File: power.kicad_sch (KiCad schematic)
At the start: 27 parts, among them Q1 CSD17311Q5, Q2 CSD17311Q5, U10 DS4432U+, U9 TPS40305

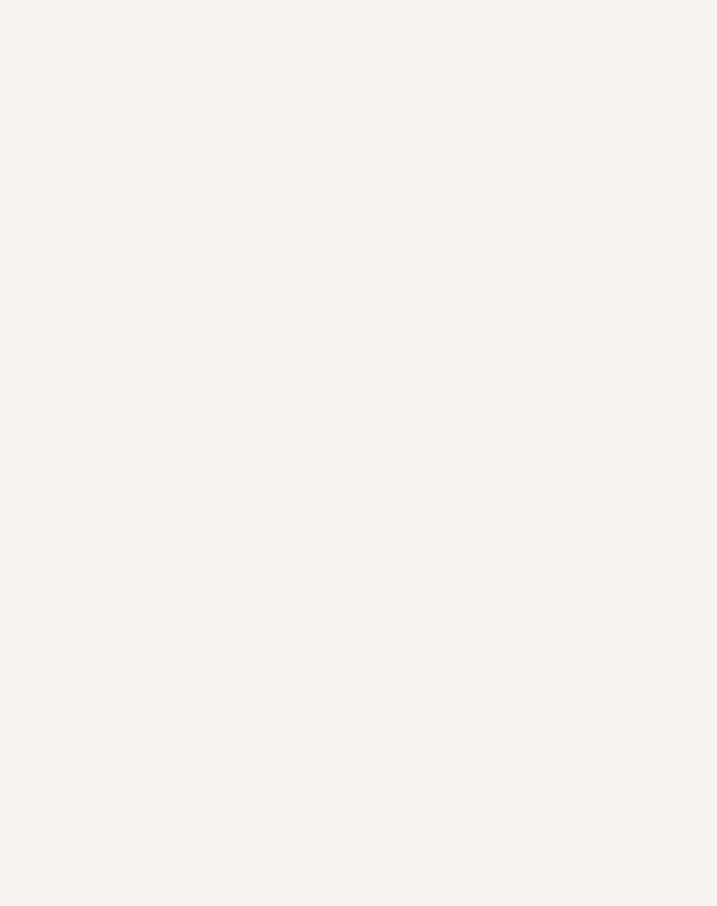
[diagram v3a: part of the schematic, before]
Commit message: started on new LM5085 based buck design
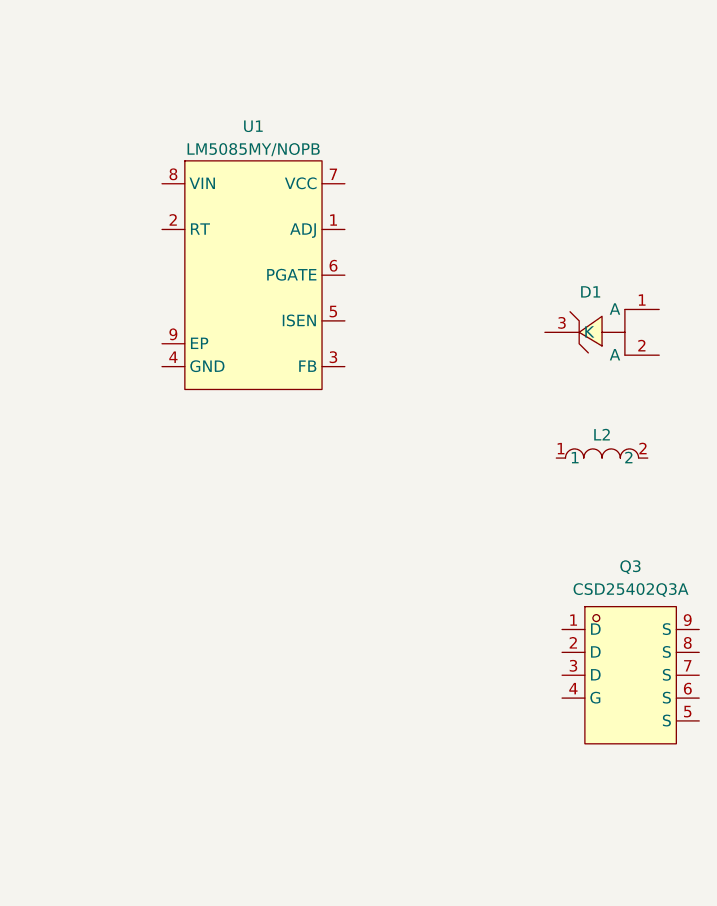
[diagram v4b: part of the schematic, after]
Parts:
- added D1: FSV1045V, lcsc:TO-277A_L6.1-W4.6-P2.13-LS6.5-TR, symbol lcsc:FSV1045V
- added L2: IHLP4040DZER1R0M01, lcsc:IND-SMD_L10.2-W10.2-LS10.8, symbol lcsc:IHLP4040DZER1R0M01
- added Q3: CSD25402Q3A, lcsc:VSONP-8_L3.1-W3.1-P0.65-LS3.5-BL, symbol lcsc:CSD25402Q3A
- added U1: LM5085MY/NOPB, lcsc:MSOP-8_L3.0-W3.0-P0.65-LS5.0-BL-EP, symbol lcsc:LM5085MY_NOPB
- U9: LCSC Part (none) -> C140285
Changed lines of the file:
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@@
+    )
+  )
+  (symbol (lib_id "lcsc:IHLP4040DZER1R0M01") (at 433.705 71.755 0) (unit 1)
+    (in_bom yes) (on_board yes) (dnp no)
+    (property "Reference" "L2" (at 433.705 69.215 0)
+      (effects (font (size 1.27 1.27)))
+    )
+    (property "Value" "IHLP4040DZER1R0M01" (at 433.705 68.58 0)
+      (effects (font (size 1.27 1.27)) hide)
+    )
+    (property "Footprint" "lcsc:IND-SMD_L10.2-W10.2-LS10.8" (at 433.705 79.375 0)
+      (effects (font (size 1.27 1.27)) hide)
+    )
+    (property "Datasheet" "" (at 433.705 71.755 0)
+      (effects (font (size 1.27 1.27)) hide)
+    )
+    (property "Manufacturer" "VISHAY(威世)" (at 433.705 81.915 0)
+      (effects (font (size 1.27 1.27)) hide)
+    )
+    (property "LCSC Part" "C845068" (at 433.705 84.455 0)
+      (effects (font (size 1.27 1.27)) hide)
+    )
+    (pin "1")
+    (pin "2")
+    (instances
+      (project "Hashat"
+        (path "/00740941-7ad8-466a-a267-188591e2b5c4/a06b4d76-7549-4f87-b16c-eb4e8ad457b9"
+          (reference "L2") (unit 1)
+        )
+      )
     )
   )
@@
         (path "/e63e39d7-6ac0-4ffd-8aa3-1841a4541b55/8ec0a9c6-2b78-44ef-a83d-9047d2828409"
           (reference "C40") (unit 1)
+        )
+      )
+    )
+  )
+  (symbol (lib_id "lcsc:FSV1045V") (at 433.705 57.785 0) (unit 1)
+    (in_bom yes) (on_board yes) (dnp no)
+    (property "Reference" "D1" (at 432.435 53.34 0)
+      (effects (font (size 1.27 1.27)))
+    )
+    (property "Value" "FSV1045V" (at 432.435 52.07 0)
+      (effects (font (size 1.27 1.27)) hide)
+    )
+    (property "Footprint" "lcsc:TO-277A_L6.1-W4.6-P2.13-LS6.5-TR" (at 433.705 67.945 0)
+      (effects (font (size 1.27 1.27)) hide)
+    )
+    (property "Datasheet" "" (at 433.705 57.785 0)
+      (effects (font (size 1.27 1.27)) hide)
+    )
+    (property "Manufacturer" "onsemi(安森美)" (at 433.705 70.485 0)
+      (effects (font (size 1.27 1.27)) hide)
+    )
+    (property "LCSC Part" "C895433" (at 433.705 73.025 0)
+      (effects (font (size 1.27 1.27)) hide)
+    )
+    (property "JLC Part" "Extended Part" (at 433.705 75.565 0)
+      (effects (font (size 1.27 1.27)) hide)
+    )
+    (pin "1")
+    (pin "2")
+    (pin "3")
+    (instances
+      (project "Hashat"
+        (path "/00740941-7ad8-466a-a267-188591e2b5c4/a06b4d76-7549-4f87-b16c-eb4e8ad457b9"
+          (reference "D1") (unit 1)
         )
       )
@@
     )
     (property "PARTNO" "TPS40305DRCR" (at 127.635 45.72 0)
+      (effects (font (size 1.27 1.27)) hide)
+    )
+    (property "LCSC Part" "C140285" (at 127.635 45.72 0)
       (effects (font (size 1.27 1.27)) hide)
     )
@@
         )
       )
+    )
+  )
+  (symbol (lib_id "lcsc:LM5085MY_NOPB") (at 396.24 51.435 0) (unit 1)
+    (in_bom yes) (on_board yes) (dnp no)
+    (property "Reference" "U1" (at 394.97 34.925 0)
+      (effects (font (size 1.27 1.27)))
+    )
+    (property "Value" "LM5085MY/NOPB" (at 394.97 37.465 0)
+      (effects (font (size 1.27 1.27)))
+    )
+    (property "Footprint" "lcsc:MSOP-8_L3.0-W3.0-P0.65-LS5.0-BL-EP" (at 396.24 69.215 0)
+      (effects (font (size 1.27 1.27)) hide)
+    )
+    (property "Datasheet" "https://lcsc.com/product-detail/DC-DC-Converters_NS_LM5085MY-NOPB_LM5085MY-NOPB_C79823.html" (at 396.24 71.755 0)
+      (effects (font (size 1.27 1.27)) hide)
+    )
+    (property "Manufacturer" "TI(德州仪器)" (at 396.24 74.295 0)
+      (effects (font (size 1.27 1.27)) hide)
+    )
+    (property "LCSC Part" "C79823" (at 396.24 76.835 0)
+      (effects (font (size 1.27 1.27)) hide)
+    )
+    (property "JLC Part" "Extended Part" (at 396.24 79.375 0)
+      (effects (font (size 1.27 1.27)) hide)
+    )
+    (pin "1")
+    (pin "2")
+    (pin "3")
+    (pin "4")
+    (pin "5")
+    (pin "6")
+    (pin "7")
+    (pin "8")
+    (pin "9")
+    (instances
+      (project "Hashat"
+        (path "/00740941-7ad8-466a-a267-188591e2b5c4/a06b4d76-7549-4f87-b16c-eb4e8ad457b9"
+          (reference "U1") (unit 1)
+        )
+      )
+    )
+  )
+  (symbol (lib_id "lcsc:CSD25402Q3A") (at 434.34 95.885 0) (unit 1)
+    (in_bom yes) (on_board yes) (dnp no)
+    (property "Reference" "Q3" (at 436.88 83.82 0)
+      (effects (font (size 1.27 1.27)))
+    )
+    (property "Value" "CSD25402Q3A" (at 436.88 86.36 0)
+      (effects (font (size 1.27 1.27)))
+    )
+    (property "Footprint" "lcsc:VSONP-8_L3.1-W3.1-P0.65-LS3.5-BL" (at 434.34 108.585 0)
+      (effects (font (size 1.27 1.27)) hide)
+    )
+    (property "Datasheet" "https://lcsc.com/product-detail/MOSFET_TI_CSD25402Q3A_CSD25402Q3A_C111356.html" (at 434.34 111.125 0)
+      (effects (font (size 1.27 1.27)) hide)
+    )
+    (property "Manufacturer" "TI(德州仪器)" (at 434.34 113.665 0)
+      (effects (font (size 1.27 1.27)) hide)
+    )
+    (property "LCSC Part" "C111356" (at 434.34 116.205 0)
+      (effects (font (size 1.27 1.27)) hide)
+    )
+    (property "JLC Part" "Extended Part" (at 434.34 118.745 0)
+      (effects (font (size 1.27 1.27)) hide)
+    )
+    (pin "1")
+    (pin "2")
+    (pin "3")
+    (pin "4")
+    (pin "5")
+    (pin "6")
+    (pin "7")
+    (pin "8")
+    (pin "9")
+    (instances
+      (project "Hashat"
+        (path "/00740941-7ad8-466a-a267-188591e2b5c4/a06b4d76-7549-4f87-b16c-eb4e8ad457b9"
+          (reference "Q3") (unit 1)
+        )
+      )

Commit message: cleanup level shifters. LCRC inductor for buck
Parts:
- removed D1: FSV1045V, lcsc:TO-277A_L6.1-W4.6-P2.13-LS6.5-TR, symbol lcsc:FSV1045V
- removed L1: 150nH, TPS40305_supply:FP1005R1-R15-R, symbol Device:L
- removed L2: IHLP4040DZER1R0M01, lcsc:IND-SMD_L10.2-W10.2-LS10.8, symbol lcsc:IHLP4040DZER1R0M01
- removed Q3: CSD25402Q3A, lcsc:VSONP-8_L3.1-W3.1-P0.65-LS3.5-BL, symbol lcsc:CSD25402Q3A
- removed U1: LM5085MY/NOPB, lcsc:MSOP-8_L3.0-W3.0-P0.65-LS5.0-BL-EP, symbol lcsc:LM5085MY_NOPB
- added U1: 220nH, lcsc:IND-SMD_L13.5-W12.8, symbol lcsc:XR1240-R22M
- DC1: Manufacturer G-Switch -> G-Switch(品赞)
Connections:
- net SW: now also U1.1
- net VOUT: now also U1.2
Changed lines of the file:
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@@
   (junction (at 187.96 45.085) (diameter 0) (color 0 0 0 0)
   )
+  (junction (at 207.01 41.91) (diameter 0) (color 0 0 0 0)
+  )
   (junction (at 100.33 73.66) (diameter 0) (color 0 0 0 0)
   )
-  (junction (at 207.01 41.91) (diameter 0) (color 0 0 0 0)
-  )
   (junction (at 217.805 64.135) (diameter 0) (color 0 0 0 0)
   )
@@
     (stroke (width 0) (type default))
   )
+  (wire (pts (xy 200.66 41.91) (xy 207.01 41.91))
+    (stroke (width 0) (type default))
+  )
   (wire (pts (xy 158.75 58.42) (xy 158.75 53.34))
     (stroke (width 0) (type default))
@@
   )
   (wire (pts (xy 207.01 62.23) (xy 207.01 64.135))
-    (stroke (width 0) (type default))
-  )
-  (wire (pts (xy 198.12 41.91) (xy 207.01 41.91))
     (stroke (width 0) (type default))
   )
@@
     )
   )
-  (symbol (lib_id "lcsc:IHLP4040DZER1R0M01") (at 433.705 71.755 0) (unit 1)
-    (in_bom yes) (on_board yes) (dnp no)
-    (property "Reference" "L2" (at 433.705 69.215 0)
-      (effects (font (size 1.27 1.27)))
-    )
-    (property "Value" "IHLP4040DZER1R0M01" (at 433.705 68.58 0)
-      (effects (font (size 1.27 1.27)) hide)
-    )
-    (property "Footprint" "lcsc:IND-SMD_L10.2-W10.2-LS10.8" (at 433.705 79.375 0)
-      (effects (font (size 1.27 1.27)) hide)
-    )
-    (property "Datasheet" "" (at 433.705 71.755 0)
-      (effects (font (size 1.27 1.27)) hide)
-    )
-    (property "Manufacturer" "VISHAY(威世)" (at 433.705 81.915 0)
-      (effects (font (size 1.27 1.27)) hide)
-    )
-    (property "LCSC Part" "C845068" (at 433.705 84.455 0)
-      (effects (font (size 1.27 1.27)) hide)
-    )
-    (pin "1")
-    (pin "2")
-    (instances
-      (project "Hashat"
-        (path "/00740941-7ad8-466a-a267-188591e2b5c4/a06b4d76-7549-4f87-b16c-eb4e8ad457b9"
-          (reference "L2") (unit 1)
-        )
-      )
-    )
-  )
   (symbol (lib_id "Device:C") (at 92.71 63.5 0) (unit 1)
     (in_bom yes) (on_board yes) (dnp no)
@@
     )
   )
-  (symbol (lib_id "lcsc:FSV1045V") (at 433.705 57.785 0) (unit 1)
-    (in_bom yes) (on_board yes) (dnp no)
-    (property "Reference" "D1" (at 432.435 53.34 0)
-      (effects (font (size 1.27 1.27)))
-    )
-    (property "Value" "FSV1045V" (at 432.435 52.07 0)
-      (effects (font (size 1.27 1.27)) hide)
-    )
-    (property "Footprint" "lcsc:TO-277A_L6.1-W4.6-P2.13-LS6.5-TR" (at 433.705 67.945 0)
-      (effects (font (size 1.27 1.27)) hide)
-    )
-    (property "Datasheet" "" (at 433.705 57.785 0)
-      (effects (font (size 1.27 1.27)) hide)
-    )
-    (property "Manufacturer" "onsemi(安森美)" (at 433.705 70.485 0)
-      (effects (font (size 1.27 1.27)) hide)
-    )
-    (property "LCSC Part" "C895433" (at 433.705 73.025 0)
-      (effects (font (size 1.27 1.27)) hide)
-    )
-    (property "JLC Part" "Extended Part" (at 433.705 75.565 0)
-      (effects (font (size 1.27 1.27)) hide)
-    )
-    (pin "1")
-    (pin "2")
-    (pin "3")
-    (instances
-      (project "Hashat"
-        (path "/00740941-7ad8-466a-a267-188591e2b5c4/a06b4d76-7549-4f87-b16c-eb4e8ad457b9"
-          (reference "D1") (unit 1)
-        )
-      )
-    )
-  )
   (symbol (lib_id "Device:C") (at 162.56 62.23 0) (unit 1)
     (in_bom yes) (on_board yes) (dnp no) (fields_autoplaced)
@@
         (path "/e63e39d7-6ac0-4ffd-8aa3-1841a4541b55/8ec0a9c6-2b78-44ef-a83d-9047d2828409"
           (reference "R10") (unit 1)
+        )
+      )
+    )
+  )
+  (symbol (lib_id "lcsc:XR1240-R22M") (at 195.58 41.91 0) (unit 1)
+    (in_bom yes) (on_board yes) (dnp no)
+    (property "Reference" "U1" (at 195.58 39.37 0)
+      (effects (font (size 1.27 1.27)))
+    )
+    (property "Value" "220nH" (at 196.215 43.815 0)
+      (effects (font (size 1.27 1.27)))
+    )
+    (property "Footprint" "lcsc:IND-SMD_L13.5-W12.8" (at 195.58 49.53 0)
+      (effects (font (size 1.27 1.27)) hide)
+    )
+    (property "Datasheet" "" (at 195.58 41.91 0)
+      (effects (font (size 1.27 1.27)) hide)
+    )
+    (property "Manufacturer" "XR(祥如)" (at 195.58 52.07 0)
+      (effects (font (size 1.27 1.27)) hide)
+    )
+    (property "LCSC Part" "C5339445" (at 195.58 54.61 0)
+      (effects (font (size 1.27 1.27)) hide)
+    )
+    (property "PARTNO" "XR1240-R22M" (at 195.58 41.91 0)
+      (effects (font (size 1.27 1.27)) hide)
+    )
+    (pin "1")
+    (pin "2")
+    (instances
+      (project "Hashat"
+        (path "/00740941-7ad8-466a-a267-188591e2b5c4/a06b4d76-7549-4f87-b16c-eb4e8ad457b9"
+          (reference "U1") (unit 1)
         )
       )
@@
     )
   )
-  (symbol (lib_id "Device:L") (at 194.31 41.91 90) (unit 1)
-    (in_bom yes) (on_board yes) (dnp no)
-    (property "Reference" "L1" (at 191.135 40.005 90)
-      (effects (font (size 1.27 1.27)))
-    )
-    (property "Value" "150nH" (at 200.66 40.005 90)
-      (effects (font (size 1.27 1.27)))
-    )
-    (property "Footprint" "TPS40305_supply:FP1005R1-R15-R" (at 194.31 41.91 0)
-      (effects (font (size 1.27 1.27)) hide)
-    )
-    (property "Datasheet" "https://www.eaton.com/content/dam/eaton/products/electronic-components/resources/data-sheet/eaton-fp1005r-high-current-power-inductors-data-sheet.pdf" (at 194.31 41.91 0)
-      (effects (font (size 1.27 1.27)) hide)
-    )
-    (property "PARTNO" "FP1005R1-R15-R" (at 194.31 41.91 90)
-      (effects (font (size 1.27 1.27)) hide)
-    )
-    (property "DK" "513-1568-1-ND" (at 194.31 41.91 90)
-      (effects (font (size 1.27 1.27)) hide)
-    )
-    (property "LCSC Part" "C2453377" (at 194.31 41.91 90)
-      (effects (font (size 1.27 1.27)) hide)
-    )
-    (pin "1")
-    (pin "2")
-    (instances
-      (project "Hashat"
-        (path "/00740941-7ad8-466a-a267-188591e2b5c4/a06b4d76-7549-4f87-b16c-eb4e8ad457b9"
-          (reference "L1") (unit 1)
-        )
-      )
-      (project "bitaxeMax"
-        (path "/e63e39d7-6ac0-4ffd-8aa3-1841a4541b55/8ec0a9c6-2b78-44ef-a83d-9047d2828409"
-          (reference "L1") (unit 1)
-        )
-      )
-    )
-  )
   (symbol (lib_id "Device:C") (at 150.495 40.005 0) (unit 1)
     (in_bom yes) (on_board yes) (dnp no) (fields_autoplaced)
@@
       (effects (font (size 1.27 1.27)) hide)
     )
-    (property "Manufacturer" "G-Switch" (at 44.45 129.54 0)
+    (property "Manufacturer" "G-Switch(品赞)" (at 44.45 129.54 0)
       (effects (font (size 1.27 1.27)) hide)
     )
@@
         )
       )
-    )
-  )
-  (symbol (lib_id "lcsc:LM5085MY_NOPB") (at 396.24 51.435 0) (unit 1)
-    (in_bom yes) (on_board yes) (dnp no)
-    (property "Reference" "U1" (at 394.97 34.925 0)
-      (effects (font (size 1.27 1.27)))
-    )
-    (property "Value" "LM5085MY/NOPB" (at 394.97 37.465 0)
-      (effects (font (size 1.27 1.27)))
-    )
-    (property "Footprint" "lcsc:MSOP-8_L3.0-W3.0-P0.65-LS5.0-BL-EP" (at 396.24 69.215 0)
-      (effects (font (size 1.27 1.27)) hide)
-    )
-    (property "Datasheet" "https://lcsc.com/product-detail/DC-DC-Converters_NS_LM5085MY-NOPB_LM5085MY-NOPB_C79823.html" (at 396.24 71.755 0)
-      (effects (font (size 1.27 1.27)) hide)
-    )
-    (property "Manufacturer" "TI(德州仪器)" (at 396.24 74.295 0)
-      (effects (font (size 1.27 1.27)) hide)
-    )
-    (property "LCSC Part" "C79823" (at 396.24 76.835 0)
-      (effects (font (size 1.27 1.27)) hide)
-    )
-    (property "JLC Part" "Extended Part" (at 396.24 79.375 0)
-      (effects (font (size 1.27 1.27)) hide)
-    )
-    (pin "1")
-    (pin "2")
-    (pin "3")
-    (pin "4")
-    (pin "5")
-    (pin "6")
-    (pin "7")
-    (pin "8")
-    (pin "9")
-    (instances
-      (project "Hashat"
-        (path "/00740941-7ad8-466a-a267-188591e2b5c4/a06b4d76-7549-4f87-b16c-eb4e8ad457b9"
-          (reference "U1") (unit 1)
-        )
-      )
-    )
-  )
-  (symbol (lib_id "lcsc:CSD25402Q3A") (at 434.34 95.885 0) (unit 1)
-    (in_bom yes) (on_board yes) (dnp no)
-    (property "Reference" "Q3" (at 436.88 83.82 0)
-      (effects (font (size 1.27 1.27)))
-    )
-    (property "Value" "CSD25402Q3A" (at 436.88 86.36 0)
-      (effects (font (size 1.27 1.27)))
-    )
-    (property "Footprint" "lcsc:VSONP-8_L3.1-W3.1-P0.65-LS3.5-BL" (at 434.34 108.585 0)
-      (effects (font (size 1.27 1.27)) hide)
-    )
-    (property "Datasheet" "https://lcsc.com/product-detail/MOSFET_TI_CSD25402Q3A_CSD25402Q3A_C111356.html" (at 434.34 111.125 0)
-      (effects (font (size 1.27 1.27)) hide)
-    )
-    (property "Manufacturer" "TI(德州仪器)" (at 434.34 113.665 0)
-      (effects (font (size 1.27 1.27)) hide)
-    )
-    (property "LCSC Part" "C111356" (at 434.34 116.205 0)
-      (effects (font (size 1.27 1.27)) hide)
-    )
-    (property "JLC Part" "Extended Part" (at 434.34 118.745 0)
-      (effects (font (size 1.27 1.27)) hide)
-    )
-    (pin "1")
-    (pin "2")
-    (pin "3")
-    (pin "4")
-    (pin "5")
-    (pin "6")
-    (pin "7")
-    (pin "8")
-    (pin "9")
-    (instances
-      (project "Hashat"
-        (path "/00740941-7ad8-466a-a267-188591e2b5c4/a06b4d76-7549-4f87-b16c-eb4e8ad457b9"
-          (reference "Q3") (unit 1)
-        )
-      )

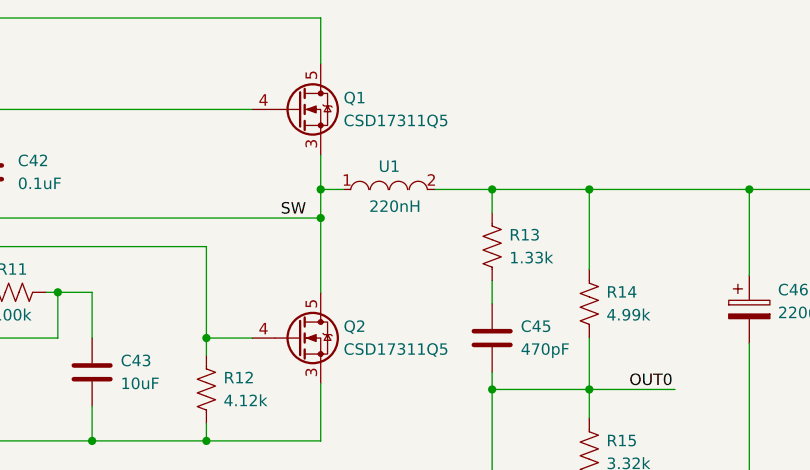
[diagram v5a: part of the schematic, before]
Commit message: adding 3D models. lots of placement. a little routing started
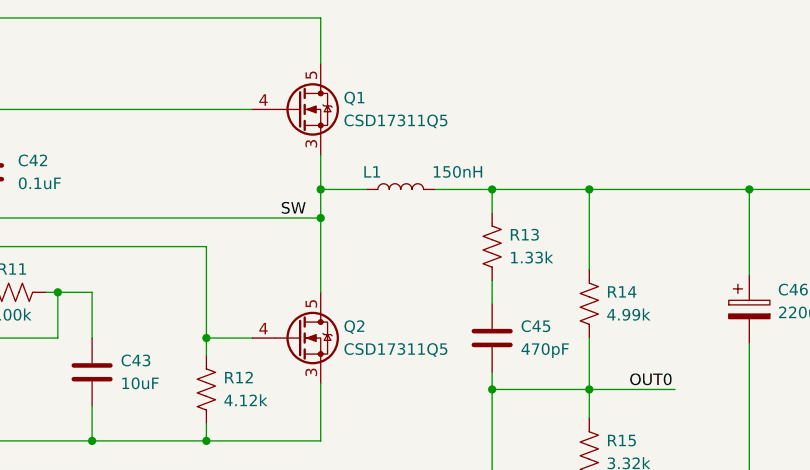
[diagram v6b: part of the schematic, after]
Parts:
- removed U1: 220nH, lcsc:IND-SMD_L13.5-W12.8, symbol lcsc:XR1240-R22M
- added L1: 150nH, TPS40305_supply:FP1005R1-R15-R, symbol Device:L
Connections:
- net SW: now also L1.1
- net VOUT: now also L1.2
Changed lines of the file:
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@@
     (stroke (width 0) (type default))
   )
-  (wire (pts (xy 187.96 41.91) (xy 190.5 41.91))
+  (wire (pts (xy 187.96 41.91) (xy 193.04 41.91))
     (stroke (width 0) (type default))
   )
@@
         (path "/e63e39d7-6ac0-4ffd-8aa3-1841a4541b55/8ec0a9c6-2b78-44ef-a83d-9047d2828409"
           (reference "R10") (unit 1)
-        )
-      )
-    )
-  )
-  (symbol (lib_id "lcsc:XR1240-R22M") (at 195.58 41.91 0) (unit 1)
-    (in_bom yes) (on_board yes) (dnp no)
-    (property "Reference" "U1" (at 195.58 39.37 0)
-      (effects (font (size 1.27 1.27)))
-    )
-    (property "Value" "220nH" (at 196.215 43.815 0)
-      (effects (font (size 1.27 1.27)))
-    )
-    (property "Footprint" "lcsc:IND-SMD_L13.5-W12.8" (at 195.58 49.53 0)
-      (effects (font (size 1.27 1.27)) hide)
-    )
-    (property "Datasheet" "" (at 195.58 41.91 0)
-      (effects (font (size 1.27 1.27)) hide)
-    )
-    (property "Manufacturer" "XR(祥如)" (at 195.58 52.07 0)
-      (effects (font (size 1.27 1.27)) hide)
-    )
-    (property "LCSC Part" "C5339445" (at 195.58 54.61 0)
-      (effects (font (size 1.27 1.27)) hide)
-    )
-    (property "PARTNO" "XR1240-R22M" (at 195.58 41.91 0)
-      (effects (font (size 1.27 1.27)) hide)
-    )
-    (pin "1")
-    (pin "2")
-    (instances
-      (project "Hashat"
-        (path "/00740941-7ad8-466a-a267-188591e2b5c4/a06b4d76-7549-4f87-b16c-eb4e8ad457b9"
-          (reference "U1") (unit 1)
         )
       )
@@
         )
       )
+    )
+  )
+  (symbol (lib_id "Device:L") (at 196.85 41.91 90) (unit 1)
+    (in_bom yes) (on_board yes) (dnp no)
+    (property "Reference" "L1" (at 193.675 40.005 90)
+      (effects (font (size 1.27 1.27)))
+    )
+    (property "Value" "150nH" (at 203.2 40.005 90)
+      (effects (font (size 1.27 1.27)))
+    )
+    (property "Footprint" "TPS40305_supply:FP1005R1-R15-R" (at 196.85 41.91 0)
+      (effects (font (size 1.27 1.27)) hide)
+    )
+    (property "Datasheet" "https://www.eaton.com/content/dam/eaton/products/electronic-components/resources/data-sheet/eaton-fp1005r-high-current-power-inductors-data-sheet.pdf" (at 196.85 41.91 0)
+      (effects (font (size 1.27 1.27)) hide)
+    )
+    (property "PARTNO" "FP1005R1-R15-R" (at 196.85 41.91 90)
+      (effects (font (size 1.27 1.27)) hide)
+    )
+    (property "DK" "513-1568-1-ND" (at 196.85 41.91 90)
+      (effects (font (size 1.27 1.27)) hide)
+    )
+    (pin "1")
+    (pin "2")
+    (instances
+      (project "Hashat"
+        (path "/00740941-7ad8-466a-a267-188591e2b5c4/a06b4d76-7549-4f87-b16c-eb4e8ad457b9"
+          (reference "L1") (unit 1)
+        )
+      )
+      (project "bitaxeMax"
+        (path "/e63e39d7-6ac0-4ffd-8aa3-1841a4541b55/8ec0a9c6-2b78-44ef-a83d-9047d2828409"
+          (reference "L1") (unit 1)
+        )
+      )
